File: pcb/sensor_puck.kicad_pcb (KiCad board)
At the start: 2 copper layers, 41.6 x 41.9 mm, 34 parts, among them J1 Conn_01x07_Socket, J2 Conn_01x07_Socket, J3 USB_C_Receptacle_USB2.0_16P, SW1 RST, SW2 BOOT, U1 ESP32-S3-MINI-1U, U2 LIS3MDL, U3 LSM6DSOXTR, U4 STC31-C-R3

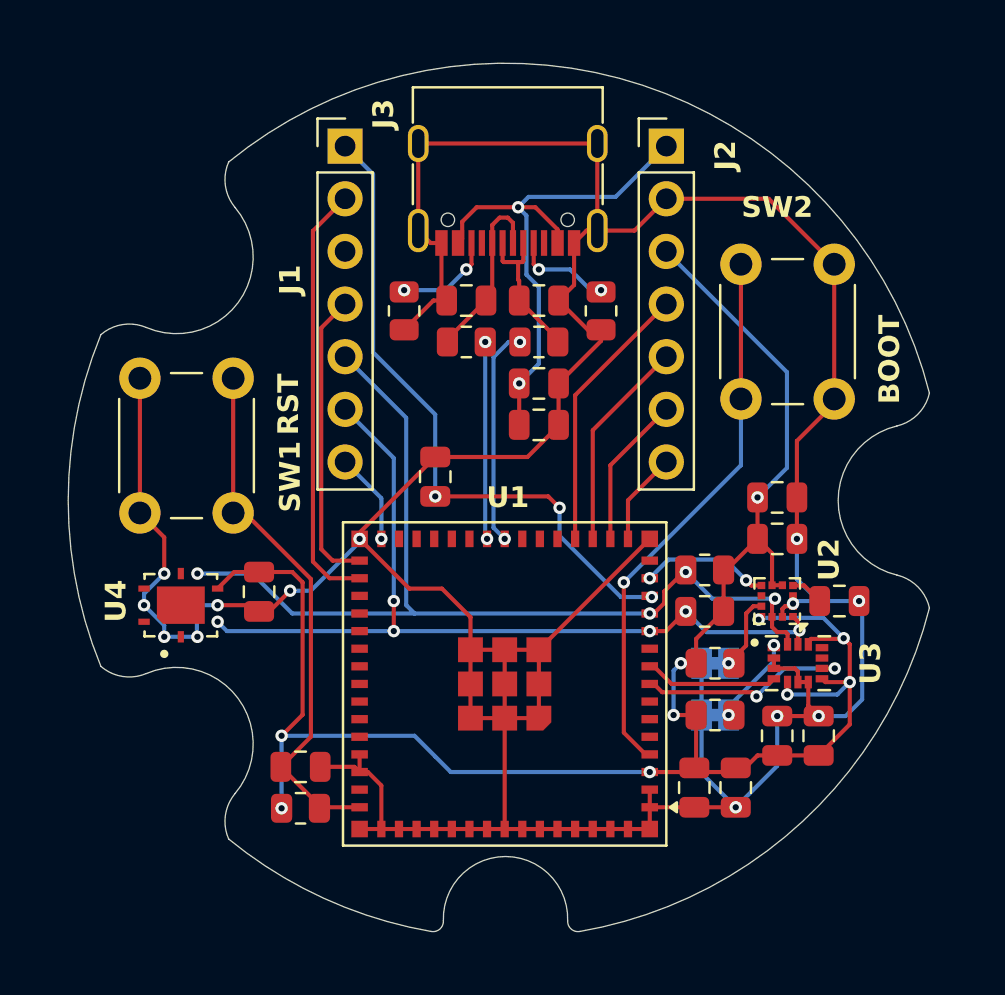
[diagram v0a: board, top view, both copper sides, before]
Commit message: feat(pcb): VBUS -> 3V3 regulator, BME288, general improvements
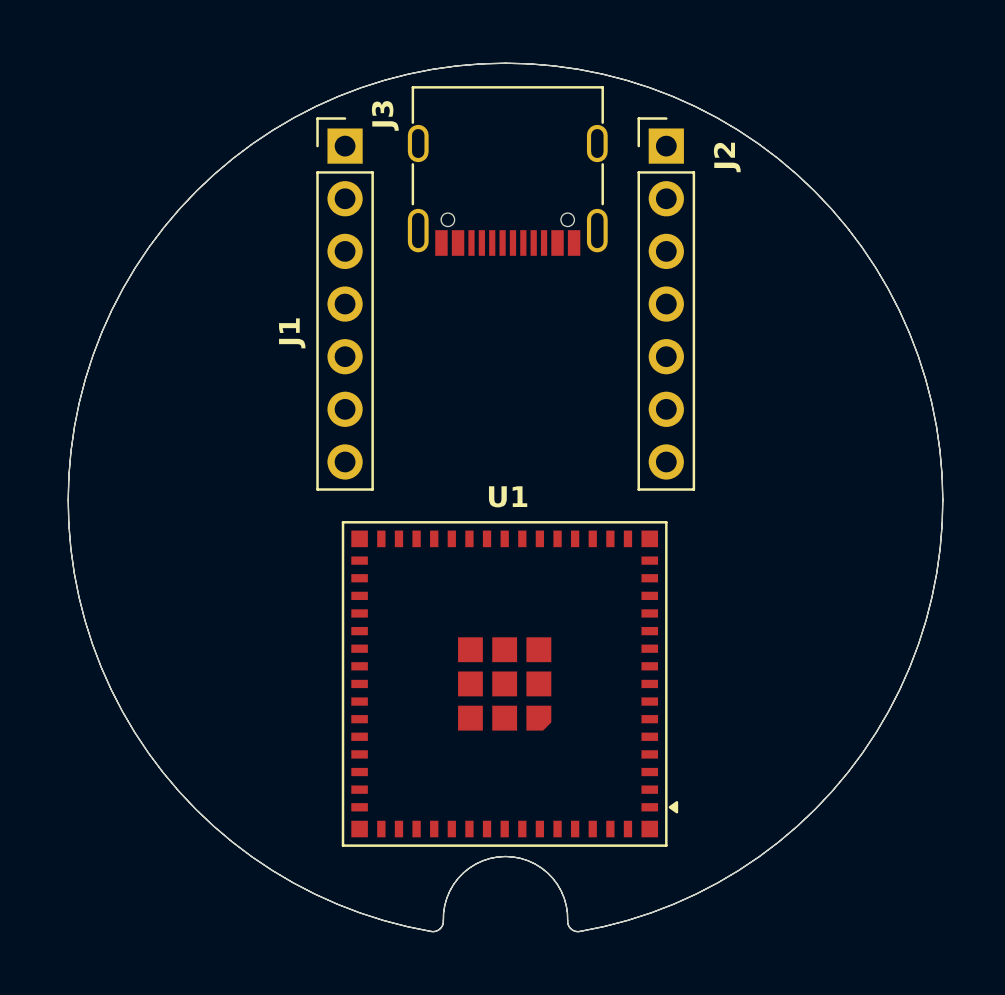
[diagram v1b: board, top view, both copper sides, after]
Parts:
- removed C1, C11, C12, C13, C14, C19, C6, C8, C9: 100nF, Capacitor_SMD:C_0805_2012Metric
- removed C10: 1uF, Capacitor_SMD:C_0805_2012Metric
- removed C17: 22uF, Capacitor_SMD:C_0805_2012Metric
- removed C4, C5: DNP, Capacitor_SMD:C_0805_2012Metric
- removed C7: 4.7uF, Capacitor_SMD:C_0805_2012Metric
- removed JP1: SA1, Jumper:SolderJumper-2_P1.3mm_Bridged_Pad1.0x1.5mm
- removed JP2: SA0, Jumper:SolderJumper-2_P1.3mm_Bridged_Pad1.0x1.5mm
- removed R1, R12, R4: 10k, Resistor_SMD:R_0805_2012Metric
- removed R2, R3: 1k8, Resistor_SMD:R_0805_2012Metric
- removed R5, R6: 5k1, Resistor_SMD:R_0805_2012Metric
- removed R8, R9: 22R, Resistor_SMD:R_0805_2012Metric
- removed SW1: RST, Button_Switch_THT:SW_PUSH_6mm
- removed SW2: BOOT, Button_Switch_THT:SW_PUSH_6mm
- removed U2: LIS3MDL, Package_LGA:LGA-12_2x2mm_P0.5mm
- removed U3: LSM6DSOXTR, LSM6DSOX:PQFN50P250X300X86-14N
- removed U4: STC31-C-R3, STC31-C:XDCR_STC31-C-R3
- J1: value Conn_01x07_Socket -> DISP LEFT
- J2: value Conn_01x07_Socket -> DISP RIGHT
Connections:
- net +5V renamed VBUS
- U1 pad 19: MOSI -> unconnected-(U1-IO15-Pad19)
- U1 pad 21: unconnected-(U1-IO17-Pad21) -> MOSI
- U1 pad 45: Net-(U1-EN) -> EN
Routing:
- net GND: track 200.3 -> 0.00 mm, vias 13 -> 0
- net +3V3: track 95.6 -> 0.00 mm, vias 10 -> 0
- net I2C_SDA: track 47.0 -> 0.00 mm, vias 4 -> 0
- net I2C_SCL: track 42.6 -> 0.00 mm, vias 6 -> 0
- net BATT_READ: track 32.1 -> 0.00 mm, vias 3 -> 0
- net VBUS: track 26.8 -> 0.00 mm, vias 2 -> 0
- net Net-(U1-IO0): track 26.6 -> 0.00 mm, vias 1 -> 0
- net Net-(U1-EN): track 26.0 -> 0.00 mm
- net LCD_CS: track 20.7 -> 0.00 mm
- net LCD_DC: track 14.4 -> 0.00 mm
- net MOSI: track 13.2 -> 0.00 mm
- net USB_D-: track 10.6 -> 0.00 mm, vias 2 -> 0
- net LSM6_INT2: track 10.4 -> 0.00 mm, vias 2 -> 0
- net MISO: track 10.3 -> 0.00 mm
- net USB_D+: track 9.76 -> 0.00 mm, vias 2 -> 0
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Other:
- board size 41.6 x 41.9 mm -> 42.2 x 41.9 mm
- board text removed: "BOOT"
- board text removed: "LIS SA1"
- board text removed: "LSM SA0"
- board text removed: "RST"

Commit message: feat(pcb): route PCB
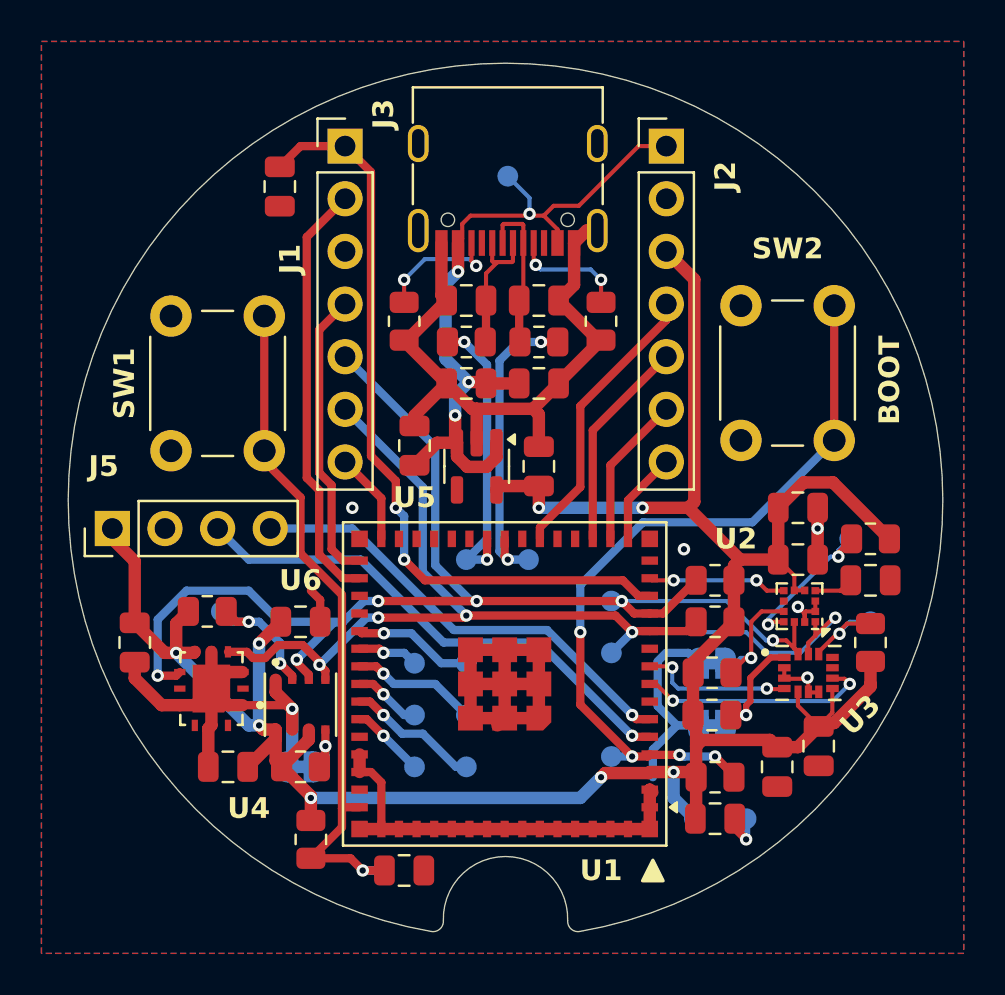
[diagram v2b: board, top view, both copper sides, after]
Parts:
- added C1: 100nF, Capacitor_SMD:C_0805_2012Metric, F.Cu at (95.0, 118.0)
- added C10: 1uF, Capacitor_SMD:C_0805_2012Metric, F.Cu at (114.0, 100.5)
- added C11: 100nF, Capacitor_SMD:C_0805_2012Metric, F.Cu at (114.0, 103.0)
- added C12: 100nF, Capacitor_SMD:C_0805_2012Metric, F.Cu at (115.0, 112.0)
- added C13: 100nF, Capacitor_SMD:C_0805_2012Metric, F.Cu at (113.0, 113.0)
- added C14: 100nF, Capacitor_SMD:C_0805_2012Metric, F.Cu at (82.0, 107.0)
- added C15: 100nF, Capacitor_SMD:C_0805_2012Metric, F.Cu at (90.0, 106.0)
- added C16: 100nF, Capacitor_SMD:C_0805_2012Metric, F.Cu at (86.5, 113.0)
- added C19: 100nF, Capacitor_SMD:C_0805_2012Metric, F.Cu at (110.0, 115.5)
- added C2: 1uF/X7R, Capacitor_SMD:C_0805_2012Metric, F.Cu at (101.5, 98.5)
- added C3: 1uF/X7R, Capacitor_SMD:C_0805_2012Metric, F.Cu at (95.5, 97.5)
- added C4: DNP, Capacitor_SMD:C_0805_2012Metric, F.Cu at (98.0, 90.5)
- added C5: DNP, Capacitor_SMD:C_0805_2012Metric, F.Cu at (101.5, 90.5)
- added C6: 100nF, Capacitor_SMD:C_0805_2012Metric, F.Cu at (98.0, 94.5)
- added C7: 4.7uF, Capacitor_SMD:C_0805_2012Metric, F.Cu at (101.5, 94.5)
- added C8: 100nF, Capacitor_SMD:C_0805_2012Metric, F.Cu at (89.0, 85.0)
- added C9: 100nF, Capacitor_SMD:C_0805_2012Metric, F.Cu at (117.5, 104.0)
- added J5: Generic, Connector_PinHeader_2.54mm:PinHeader_1x04_P2.54mm_Vertical, F.Cu at (80.9, 101.5)
- added JP1: LIS_SA1, Jumper:SolderJumper-2_P1.3mm_Bridged_RoundedPad1.0x1.5mm, B.Cu at (109.9, 108.0)
- added JP2: LSM_SA0, Jumper:SolderJumper-2_P1.3mm_Bridged_RoundedPad1.0x1.5mm, B.Cu at (109.8, 111.0)
- added JP3: BME_SDO, Jumper:SolderJumper-2_P1.3mm_Bridged_RoundedPad1.0x1.5mm, B.Cu at (90.0, 113.0)
- added R1: 10k, Resistor_SMD:R_0805_2012Metric, F.Cu at (90.5, 116.5)
- added R10: 0R, Resistor_SMD:R_0805_2012Metric, F.Cu at (117.5, 102.0)
- added R11: 0R, Resistor_SMD:R_0805_2012Metric, F.Cu at (117.5, 107.0)
- added R12: 10k, Resistor_SMD:R_0805_2012Metric, F.Cu at (109.8, 110.5)
- added R13: 10k, Resistor_SMD:R_0805_2012Metric, F.Cu at (90.0, 113.0)
- added R14: 0R, Resistor_SMD:R_0805_2012Metric, F.Cu at (85.5, 105.5)
- added R2: 10k, Resistor_SMD:R_0805_2012Metric, F.Cu at (110.0, 106.0)
- added R3: 10k, Resistor_SMD:R_0805_2012Metric, F.Cu at (110.0, 104.0)
- added R4: 10k, Resistor_SMD:R_0805_2012Metric, F.Cu at (109.9, 108.5)
- added R5: 5k11, Resistor_SMD:R_0805_2012Metric, F.Cu at (95.0, 91.5)
- added R6: 5k11, Resistor_SMD:R_0805_2012Metric, F.Cu at (104.5, 91.5)
- added R7: 10k, Resistor_SMD:R_0805_2012Metric, F.Cu at (110.0, 113.5)
- added R8: 0, Resistor_SMD:R_0805_2012Metric, F.Cu at (101.5, 92.5)
- added R9: 0, Resistor_SMD:R_0805_2012Metric, F.Cu at (98.0, 92.5)
- added SW1: RST, Button_Switch_THT:SW_PUSH_6mm, F.Cu at (83.8, 97.8)
- added SW2: BOOT, Button_Switch_THT:SW_PUSH_6mm, F.Cu at (111.2, 97.2)
- added TP1: D-, TestPoint:TestPoint_Pad_D1.0mm, B.Cu at (101.0, 103.0)
- added TP11: TXD0, TestPoint:TestPoint_Pad_D1.0mm, B.Cu at (98.0, 113.0)
- added TP12: RXD0, TestPoint:TestPoint_Pad_D1.0mm, B.Cu at (95.5, 113.0)
- added TP13: LIS_CS, TestPoint:TestPoint_Pad_D1.0mm, B.Cu at (116.5, 102.0)
- added TP14: LSM_CS, TestPoint:TestPoint_Pad_D1.0mm, B.Cu at (117.5, 106.0)
- added TP15: BME_CSB, TestPoint:TestPoint_Pad_D1.0mm, B.Cu at (86.2, 105.5)
- added TP16: MTCK, TestPoint:TestPoint_Pad_D1.0mm, B.Cu at (98.0, 108.0)
- added TP17: MTDO, TestPoint:TestPoint_Pad_D1.0mm, B.Cu at (95.5, 108.0)
- added TP18: MTDI, TestPoint:TestPoint_Pad_D1.0mm, B.Cu at (98.0, 110.5)
- added TP19: MTMS, TestPoint:TestPoint_Pad_D1.0mm, B.Cu at (95.5, 110.5)
- added TP2: D+, TestPoint:TestPoint_Pad_D1.0mm, B.Cu at (98.0, 103.0)
- added TP3: 3V3, TestPoint:TestPoint_Pad_D1.0mm, B.Cu at (109.0, 115.5)
- added TP4: GND, TestPoint:TestPoint_Pad_D1.0mm, B.Cu at (111.5, 115.5)
- added TP5: EN, TestPoint:TestPoint_Pad_D1.0mm, B.Cu at (94.0, 118.0)
- added TP6: IO0, TestPoint:TestPoint_Pad_D1.0mm, B.Cu at (105.0, 112.5)
- added TP7: SCL, TestPoint:TestPoint_Pad_D1.0mm, B.Cu at (105.0, 107.5)
- added TP8: SDA, TestPoint:TestPoint_Pad_D1.0mm, B.Cu at (105.0, 105.0)
- added TP9: VBUS, TestPoint:TestPoint_Pad_D1.0mm, B.Cu at (100.0, 84.5)
- added U2: LIS3MDL, Package_LGA:LGA-12_2x2mm_P0.5mm, F.Cu at (114.1, 105.2)
- added U3: LSM6DSOXTR, LSM6DSOX:PQFN50P250X300X86-14N, F.Cu at (114.5, 108.5)
- added U4: STC31-C-R3, STC31-C:XDCR_STC31-C-R3, F.Cu at (85.7, 109.2)
- added U5: RT9013, Package_TO_SOT_SMD:SOT-23-5, F.Cu at (98.5, 98.5)
- added U6: BME688, BME688:IC_BME688, F.Cu at (90.0, 110.0)
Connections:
- U1 pad 35: unconnected-(U1-IO39-Pad35) -> Net-(U1-IO39)
- U1 pad 36: unconnected-(U1-IO40-Pad36) -> Net-(U1-IO40)
- U1 pad 37: unconnected-(U1-IO41-Pad37) -> Net-(U1-IO41)
- U1 pad 38: unconnected-(U1-IO42-Pad38) -> Net-(U1-IO42)
- U1 pad 39: unconnected-(U1-TXD0-Pad39) -> TXD0
- U1 pad 4: Net-(U1-IO0) -> IO0
- U1 pad 40: unconnected-(U1-RXD0-Pad40) -> RXD0
- U1 pad 45: EN -> Net-(U1-EN)
- U1 pad 5: unconnected-(U1-IO1-Pad5) -> IO1
- U1 pad 6: unconnected-(U1-IO2-Pad6) -> IO2
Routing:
- net +3V3: track 0.00 -> 122.8 mm, vias 0 -> 8
- net GND: track 0.00 -> 116.0 mm, vias 0 -> 7
- net I2C_SDA: track 0.00 -> 64.9 mm, vias 0 -> 6
- net I2C_SCL: track 0.00 -> 53.6 mm, vias 0 -> 5
- net IO0: track 0.00 -> 37.4 mm, vias 0 -> 4
- net BATT_READ: track 0.00 -> 37.3 mm, vias 0 -> 2
- net VBUS: track 0.00 -> 35.8 mm, vias 0 -> 4
- net Net-(U1-EN): track 0.00 -> 33.7 mm, vias 0 -> 1
- net IO1: track 0.00 -> 25.0 mm, vias 0 -> 1
- net IO2: track 0.00 -> 22.1 mm, vias 0 -> 1
- net LCD_CS: track 0.00 -> 20.6 mm
- net USB_D-: track 0.00 -> 15.0 mm, vias 0 -> 2
- net USB_D+: track 0.00 -> 14.2 mm, vias 0 -> 2
- net LCD_DC: track 0.00 -> 14.2 mm
- net MOSI: track 0.00 -> 13.9 mm
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- added copper zone on B.Cu, net GND
- added copper zone on F.Cu, net GND
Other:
- board text added: "3V3"
- board text added: "BME CSB"
- board text added: "BME SDO"
- board text added: "BOOT"
- board text added: "D+"
- board text added: "D-"
- board text added: "EN"
- board text added: "GND"
- board text added: "IO0"
- board text added: "LIS CS"
- board text added: "LIS SA1"
- board text added: "LSM CS"
- board text added: "LSM SA0"
- board text added: "MTCK MTDO MTDI MTMS"
- board text added: "RXD0"
- board text added: "SCL"
- board text added: "SDA"
- board text added: "TXD0"

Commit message: feat: PCB design v0.2
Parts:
- removed C11, C14, C15, C16: 100nF, Capacitor_SMD:C_0805_2012Metric
- removed J5: Generic, Connector_PinHeader_2.54mm:PinHeader_1x04_P2.54mm_Vertical
- removed JP1: LIS_SA1, Jumper:SolderJumper-2_P1.3mm_Bridged_RoundedPad1.0x1.5mm
- removed JP3: BME_SDO, Jumper:SolderJumper-2_P1.3mm_Bridged_RoundedPad1.0x1.5mm
- removed R13: 10k, Resistor_SMD:R_0805_2012Metric
- removed R14: 0R, Resistor_SMD:R_0805_2012Metric
- removed TP13: LIS_CS, TestPoint:TestPoint_Pad_D1.0mm
- removed TP14: LSM_CS, TestPoint:TestPoint_Pad_D1.0mm
- removed TP15: BME_CSB, TestPoint:TestPoint_Pad_D1.0mm
- removed TP3: 3V3, TestPoint:TestPoint_Pad_D1.0mm
- removed TP4: GND, TestPoint:TestPoint_Pad_D1.0mm
- removed TP7: SCL, TestPoint:TestPoint_Pad_D1.0mm
- removed TP8: SDA, TestPoint:TestPoint_Pad_D1.0mm
- removed TP9: VBUS, TestPoint:TestPoint_Pad_D1.0mm
- removed U6: BME688, BME688:IC_BME688
- added BZ1: Buzzer, Buzzer_Beeper:CMT-7525-80-SMT-TR, B.Cu at (85.5, 95.0)
- added C17: 220nF, Capacitor_SMD:C_0805_2012Metric, F.Cu at (116.0, 103.5)
- added C18: 100nF, Capacitor_SMD:C_0805_2012Metric, F.Cu at (118.8, 100.0)
- added C20: 100nF, Capacitor_SMD:C_0805_2012Metric, F.Cu at (118.8, 102.1)
- added C21: 10nF, Capacitor_SMD:C_0805_2012Metric, F.Cu at (118.8, 98.0)
- added D1: D, Diode_SMD:D_0805_2012Metric, F.Cu at (84.5, 89.0)
- added J6: Conn_01x02_Socket, Connector_PinHeader_2.00mm:PinHeader_1x02_P2.00mm_Vertical, F.Cu at (111.5, 93.0)
- added L1: TBD, Connector_PinHeader_2.54mm:PinHeader_1x02_P2.54mm_Vertical, F.Cu at (117.5, 94.0)
- added Q1: 2N7002, Package_TO_SOT_SMD:SOT-23, F.Cu at (87.5, 89.0)
- added R15: 10k, Resistor_SMD:R_0805_2012Metric, F.Cu at (102.5, 99.0)
- added R16: 10k, Resistor_SMD:R_0805_2012Metric, B.Cu at (98.0, 96.0)
- added R17: 10k, Resistor_SMD:R_0805_2012Metric, B.Cu at (98.0, 98.0)
- added U7: LIS2MDL, Package_LGA:LGA-12_2x2mm_P0.5mm, F.Cu at (118.5, 105.0)
- added U8: SCD41-D-R2, Sensor:Sensirion_SCD4x-1EP_10.1x10.1mm_P1.25mm_EP4.8x4.8mm, F.Cu at (89.8, 108.8)
- C10: value 1uF -> 10nF
- C4, C5: value DNP -> 1uF
- R10: value 0R -> 10k
- R11: value 0R -> 5k11
- R2, R3: moved to B.Cu
- R8: value 0 -> 10k; moved to B.Cu
- R9: value 0 -> 4R7
- SW1, SW2: footprint Button_Switch_THT:SW_PUSH_6mm -> Button_Switch_SMD:SW_Push_1P1T_NO_CK_KMR2
- U2: value LIS3MDL -> ST25DV16K-IER8C3; footprint Package_LGA:LGA-12_2x2mm_P0.5mm -> Package_DFN_QFN:DFN-8-1EP_3x2mm_P0.5mm_EP1.36x1.46mm
- U3: footprint LSM6DSOX:PQFN50P250X300X86-14N -> Package_LGA:LGA-14_3x2.5mm_P0.5mm_LayoutBorder3x4y
- U4: value STC31-C-R3 -> SGP41-D-R4; footprint STC31-C:XDCR_STC31-C-R3 -> SGP41-D-R4:XDCR_SGP41-D-R4
- moved R4 27.8 mm to (87.5, 92.0)
- moved R10 22.6 mm to (95.0, 100.0), turned to -90 degrees
- moved C5 20.8 mm to (83.5, 101.0), turned to 90 degrees
- moved SW1 20.5 mm to (93.0, 116.0), turned to 0 degrees
- moved R11 15.3 mm to (104.5, 99.0), turned to -90 degrees
- moved R8 15.2 mm to (115.5, 98.5), turned to 90 degrees
- moved C4 12.5 mm to (86.5, 95.5)
- moved R9 12.5 mm to (86.5, 97.5), turned to 180 degrees
- moved R3 9.82 mm to (107.5, 113.5), turned to -90 degrees
- moved SW2 8.75 mm to (111.5, 88.5), turned to -90 degrees
- moved U4 8.14 mm to (86.7, 101.2), turned to -90 degrees
- moved JP2 8.03 mm to (117.0, 107.3), turned to 90 degrees
- moved C13 8.00 mm to (113.0, 105.0), turned to -90 degrees
- moved TP6 8.00 mm to (113.0, 112.5)
- moved R2 7.52 mm to (109.5, 113.5), turned to 90 degrees
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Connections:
- C4 pad 1: Net-(C4-Pad1) -> Net-(U4-VDD)
- C5 pad 1: Net-(C5-Pad1) -> +3V3
- C9 pad 1: Net-(U2-C1) -> GND
- C9 pad 2: GND -> +3V3
- J1 pad 3: unconnected-(J1-Pin_3-Pad3) -> SD_CS
- J1 pad 5: I2C_SDA -> LCD_I2C_SDA
- J1 pad 6: I2C_SCL -> LCD_I2C_SCL
- J3 pad A6: Net-(C4-Pad1) -> USB_D+
- J3 pad A7: Net-(C5-Pad1) -> USB_D-
- J3 pad B6: Net-(C4-Pad1) -> USB_D+
- J3 pad B7: Net-(C5-Pad1) -> USB_D-
- R10 pad 1: +3V3 -> LCD_BL
- R10 pad 2: Net-(U2-~{CS}) -> GND
- R11 pad 1: +3V3 -> VBUS
- R11 pad 2: Net-(U3-CS) -> Net-(U1-IO18)
- R2 pad 1: I2C_SCL -> +3V3
- R2 pad 2: +3V3 -> I2C_SDA
- R3 pad 1: +3V3 -> I2C_SCL
- R3 pad 2: I2C_SDA -> +3V3
- R4 pad 1: Net-(JP1-B) -> BUZZER_EN
- R4 pad 2: +3V3 -> GND
- R8 pad 1: Net-(C5-Pad1) -> ST25DV_INT
- R8 pad 2: USB_D- -> +3V3
- R9 pad 1: USB_D+ -> Net-(U4-VDD)
- R9 pad 2: Net-(C4-Pad1) -> +3V3
- SW2 pad 1: GND -> IO0
- SW2 pad 2: IO0 -> GND
- U1 pad 10: unconnected-(U1-IO6-Pad10) -> LIS2_INT
- U1 pad 11: I2C_SCL -> LCD_I2C_SCL
- U1 pad 12: I2C_SDA -> LCD_I2C_SDA
- U1 pad 13: BATT_READ -> BUZZER_EN
- U1 pad 14: LIS3_INT -> BATT_READ
- U1 pad 15: unconnected-(U1-IO11-Pad15) -> ST25DV_INT
- U1 pad 16: TP_INT -> MISO
- U1 pad 18: MISO -> TP_INT
- U1 pad 22: unconnected-(U1-IO18-Pad22) -> Net-(U1-IO18)
- U1 pad 32: LCD_CS -> SD_CS
- U1 pad 33: unconnected-(U1-IO37-Pad33) -> LCD_CS
- U1 pad 5: IO1 -> I2C_SDA
- U1 pad 6: IO2 -> I2C_SCL
- U2 pad 1: I2C_SCL -> unconnected-(U2-V_EH-Pad1)
- U2 pad 2: GND -> Net-(U2-AC0)
- U2 pad 3: GND -> Net-(U2-AC1)
- U2 pad 4: Net-(U2-C1) -> GND
- U2 pad 5: +3V3 -> I2C_SDA
- U2 pad 6: +3V3 -> I2C_SCL
- U2 pad 7: LIS3_INT -> ST25DV_INT
- U2 pad 8: unconnected-(U2-DRDY-Pad8) -> +3V3
- U2 pad 9: Net-(JP1-B) -> unconnected-(U2-NC-Pad9)
- U3 pad 12: Net-(U3-CS) -> +3V3
- U4 pad 1: GND -> Net-(U4-VDD)
- U4 pad 2: unconnected-(U4-RESERVED-Pad2) -> GND
- U4 pad 3: GND -> I2C_SDA
- U4 pad 4: I2C_SCL -> GND
- U4 pad 5: GND -> +3V3
- U4 pad 6: +3V3 -> I2C_SCL
- U4 pad 7: I2C_SDA -> GND
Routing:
- net +3V3: track 122.8 -> 187.7 mm, vias 8 -> 13
- net GND: track 116.0 -> 66.9 mm, vias 7 -> 11
- net BUZZER_EN: track 0.00 -> 36.5 mm, vias 0 -> 2
- net LCD_I2C_SDA: track 0.00 -> 26.6 mm, vias 0 -> 1
- net LCD_I2C_SCL: track 0.00 -> 26.0 mm, vias 0 -> 2
- net IO1: track 25.0 -> 0.00 mm, vias 1 -> 0
- net IO2: track 22.1 -> 0.00 mm, vias 1 -> 0
- net SD_CS: track 0.00 -> 20.6 mm
- net Net-(U1-EN): track 33.7 -> 13.9 mm
- net I2C_SCL: track 53.6 -> 67.3 mm, vias 5 -> 7
- net ST25DV_INT: track 0.00 -> 11.1 mm, vias 0 -> 2
- net LIS2_INT: track 0.00 -> 9.83 mm, vias 0 -> 2
- net Net-(BZ1--): track 0.00 -> 9.31 mm, vias 0 -> 1
- net LSM6_INT2: track 11.3 -> 2.15 mm, vias 2 -> 0
- net Net-(U2-~{CS}): track 7.92 -> 0.00 mm, vias 2 -> 0
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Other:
- board text added: "RST"
- board text added: "Sensor Puck v0.2"
- board text removed: "3V3"
- board text removed: "BME CSB"
- board text removed: "BME SDO"
- board text removed: "GND"
- board text removed: "LIS CS"
- board text removed: "LIS SA1"
- board text removed: "LSM CS"
- board text removed: "SCL"
- board text removed: "SDA"
